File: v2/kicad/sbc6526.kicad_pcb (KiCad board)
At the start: 4 copper layers, 100 x 100 mm, 59 parts, among them J1 Conn_01x10_Female, P1 2k, P2 5k, SW1 UP, SW2 DOWN, SW3 OK, SW4 CANCEL, SW5 RESET, U1 6526, U10 74AC138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

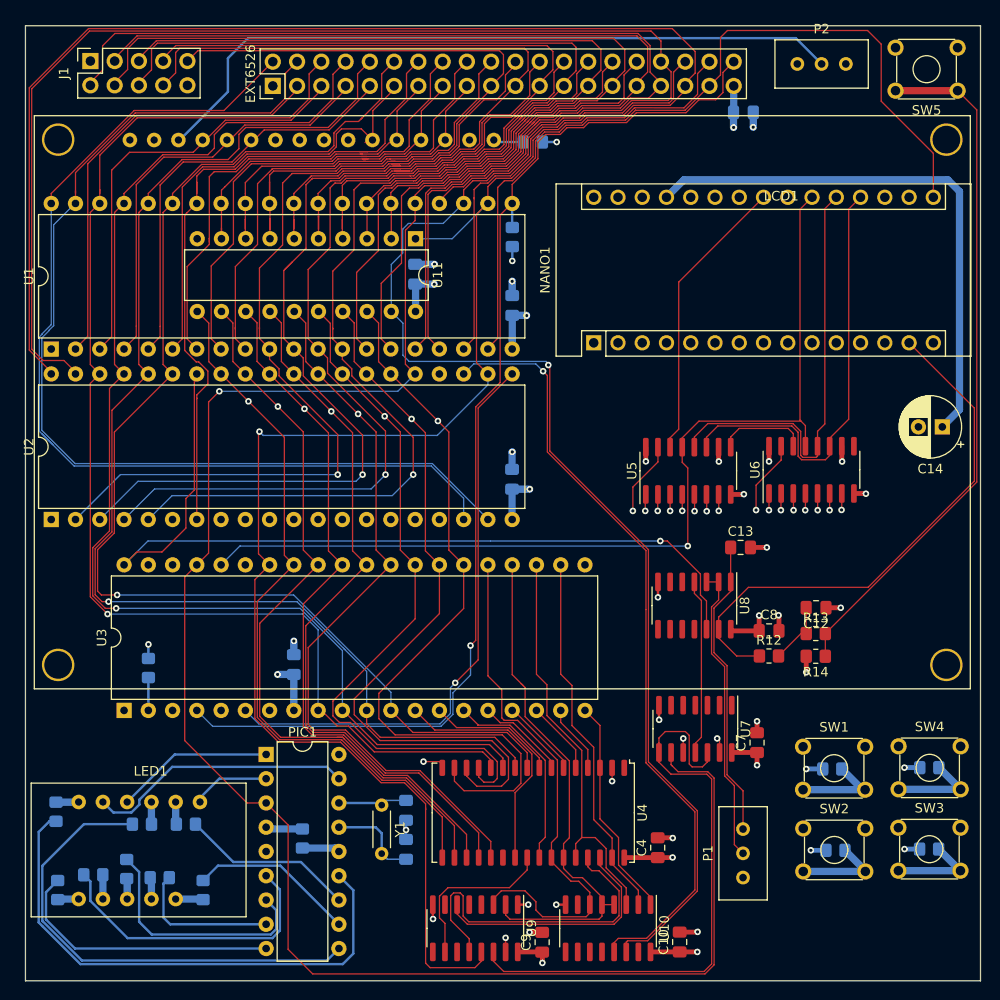
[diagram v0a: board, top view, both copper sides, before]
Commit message: All nets verified
All nets have been verified against all design. Even though v2 is not tested yet, at least, the schematic is correct.
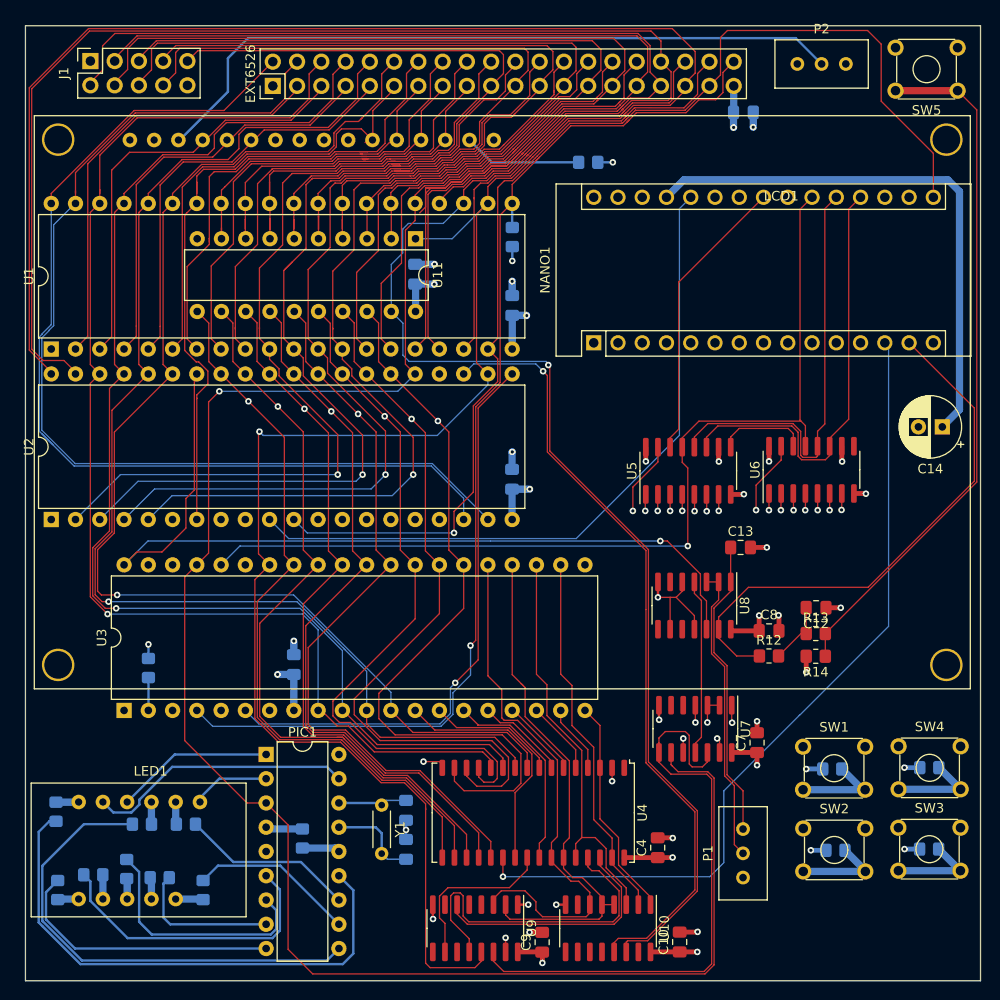
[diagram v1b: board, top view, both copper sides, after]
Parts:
- moved R10 6.18 mm to (158.9, 64.3)
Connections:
- LCD1 pad 15: GND -> Net-(LCD1-Pad15)
- LCD1 pad 16: Net-(LCD1-Pad16) -> GND
- R10 pad 2: Net-(LCD1-Pad16) -> Net-(LCD1-Pad15)
- U7 pad 1: (no net) -> VCC
- U7 pad 2: (no net) -> GND
- U7 pad 3: (no net) -> GND
- U7 pad 4: (no net) -> VCC
- U7 pad 5: (no net) -> Net-(U7-Pad5)
- U7 pad 6: (no net) -> Net-(U7-Pad6)
- U8 pad 10: (no net) -> Net-(U8-Pad10)
- U8 pad 11: (no net) -> GND
- U8 pad 5: (no net) -> GND
- U8 pad 6: (no net) -> Net-(U8-Pad6)
- U8 pad 8: (no net) -> Net-(U8-Pad8)
- U8 pad 9: (no net) -> GND
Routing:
- net /~CE: track 0.00 -> 87.5 mm, vias 0 -> 1
- net /TODENABLE: track 0.00 -> 73.6 mm
- net /TOD: track 86.5 -> 124.6 mm, vias 0 -> 1
- net /io/PB6: track 106.4 -> 121.8 mm
- net GND: track 36.2 -> 50.5 mm, vias 23 -> 24
- net Net-(LCD1-Pad15): track 0.00 -> 12.4 mm
- net VCC: track 130.0 -> 133.7 mm, vias 24 -> 26
- net Net-(LCD1-Pad16): track 3.16 -> 0.00 mm
- net /peripherals/DB6: track 35.6 -> 34.1 mm
- net /io/PB4: track 99.0 -> 97.8 mm
- net /io/PB3: track 145.0 -> 143.9 mm
- net /PHI2: track 210.0 -> 209.0 mm
- net /peripherals/DB7: track 36.1 -> 35.3 mm
- net /io/PB7: track 114.4 -> 113.5 mm
- net /peripherals/DB5: track 37.6 -> 36.8 mm
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
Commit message: new revision - dual 6526
new revision - dual 6526
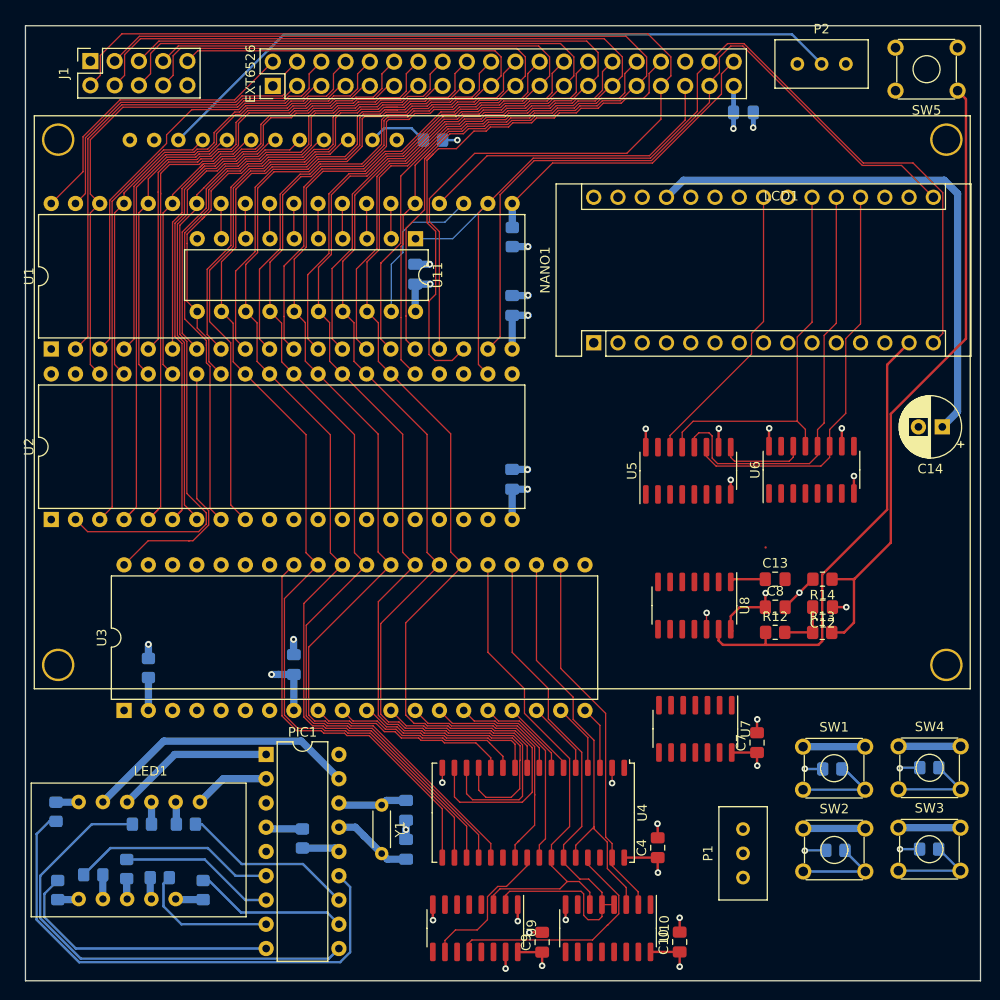
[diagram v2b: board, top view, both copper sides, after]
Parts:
- moved R10 16.4 mm to (142.7, 62.0)
- moved R14 8.10 mm to (183.4, 108.0)
- moved C13 4.92 mm to (178.5, 108.0)
- moved R12 2.56 mm to (178.5, 113.5)
- moved C8 2.56 mm to (178.5, 110.9)
- moved R13 0.68 mm to (183.4, 113.5)
- moved C12 0.68 mm to (183.5, 110.9)
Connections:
- EXT6526 pad 11: /peripherals/LCD_D4 -> /peripherals/PA4
- EXT6526 pad 13: /peripherals/LCD_D5 -> /peripherals/PA5
- EXT6526 pad 15: /peripherals/LCD_D6 -> /peripherals/PA6
- EXT6526 pad 16: /peripherals/DB0 -> /bootstrap/D0
- EXT6526 pad 17: /peripherals/LCD_D7 -> /peripherals/PA7
- EXT6526 pad 18: /peripherals/DB1 -> /bootstrap/D1
- EXT6526 pad 20: /peripherals/DB2 -> /bootstrap/D2
- EXT6526 pad 22: /peripherals/DB3 -> /bootstrap/D3
- EXT6526 pad 24: /peripherals/DB4 -> /bootstrap/D4
- EXT6526 pad 26: /peripherals/DB5 -> /bootstrap/D5
- EXT6526 pad 28: /peripherals/DB6 -> /bootstrap/D6
- EXT6526 pad 30: /peripherals/DB7 -> /bootstrap/D7
- EXT6526 pad 34: /peripherals/~FLAG -> /peripherals/~EXTPC
- EXT6526 pad 35: /peripherals/~PC -> /peripherals/~EXTFLAG
- EXT6526 pad 36: /memory/~CIA -> /memory/~CIAEXT
- EXT6526 pad 5: /peripherals/LCD_RS -> /peripherals/PA1
- EXT6526 pad 7: /peripherals/LCD_RW -> /peripherals/PA2
- EXT6526 pad 9: /peripherals/LCD_E -> /peripherals/PA3
- U1 pad 18: /peripherals/~PC -> /peripherals/~EXTPC
- U1 pad 24: /peripherals/~FLAG -> /peripherals/~EXTFLAG
- U1 pad 3: /peripherals/LCD_RS -> /peripherals/PA1
- U1 pad 4: /peripherals/LCD_RW -> /peripherals/PA2
- U1 pad 5: /peripherals/LCD_E -> /peripherals/PA3
- U1 pad 6: /peripherals/LCD_D4 -> /peripherals/PA4
- U1 pad 7: /peripherals/LCD_D5 -> /peripherals/PA5
- U1 pad 8: /peripherals/LCD_D6 -> /peripherals/PA6
- U1 pad 9: /peripherals/LCD_D7 -> /peripherals/PA7
- U10 pad 12: Net-(U10-Pad12) -> /memory/~CIAEXT
- U2 pad 18: /peripherals/SERCLK -> Net-(U2-Pad18)
- U2 pad 19: /peripherals/SERDAT -> Net-(U2-Pad19)
- U2 pad 2: /io/PB0 -> /peripherals/~CIARES
- U2 pad 3: /io/PB1 -> /peripherals/LCD_RS
- U2 pad 39: /peripherals/~FLAG -> Net-(U2-Pad39)
- U2 pad 4: /io/PB2 -> /peripherals/LCD_RW
- U2 pad 40: /peripherals/~PC -> Net-(U2-Pad40)
- U2 pad 5: /io/PB3 -> /peripherals/LCD_E
- U2 pad 6: Net-(U2-Pad6) -> /peripherals/LCD_D4
- U2 pad 7: /peripherals/~CIARES -> /peripherals/LCD_D5
- U2 pad 8: Net-(U2-Pad8) -> /peripherals/LCD_D6
- U2 pad 9: Net-(U2-Pad9) -> /peripherals/LCD_D7
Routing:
- net /PHI2: track 209.0 -> 52.6 mm, vias 1 -> 0
- net /peripherals/~PC: track 152.5 -> 0.00 mm
- net /peripherals/~FLAG: track 137.6 -> 0.00 mm
- net /memory/~CIA: track 142.0 -> 16.4 mm, vias 1 -> 0
- net /bootstrap/A0: track 187.6 -> 75.4 mm, vias 2 -> 0
- net /bootstrap/A1: track 178.2 -> 70.2 mm, vias 2 -> 0
- net /bootstrap/A3: track 177.0 -> 69.2 mm, vias 2 -> 0
- net /bootstrap/A2: track 178.4 -> 71.3 mm, vias 2 -> 0
- net /R~W: track 214.1 -> 107.2 mm, vias 1 -> 0
- net /io/VPB5: track 108.3 -> 9.72 mm
- net /io/VPB6: track 105.8 -> 9.59 mm
- net /io/VPB4: track 102.8 -> 9.72 mm
- net /~CE: track 87.5 -> 0.00 mm, vias 1 -> 0
- net /~IRQ: track 119.7 -> 33.2 mm, vias 1 -> 0
- net /io/VPB7: track 95.6 -> 9.84 mm
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
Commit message: Changing to Dual CIA
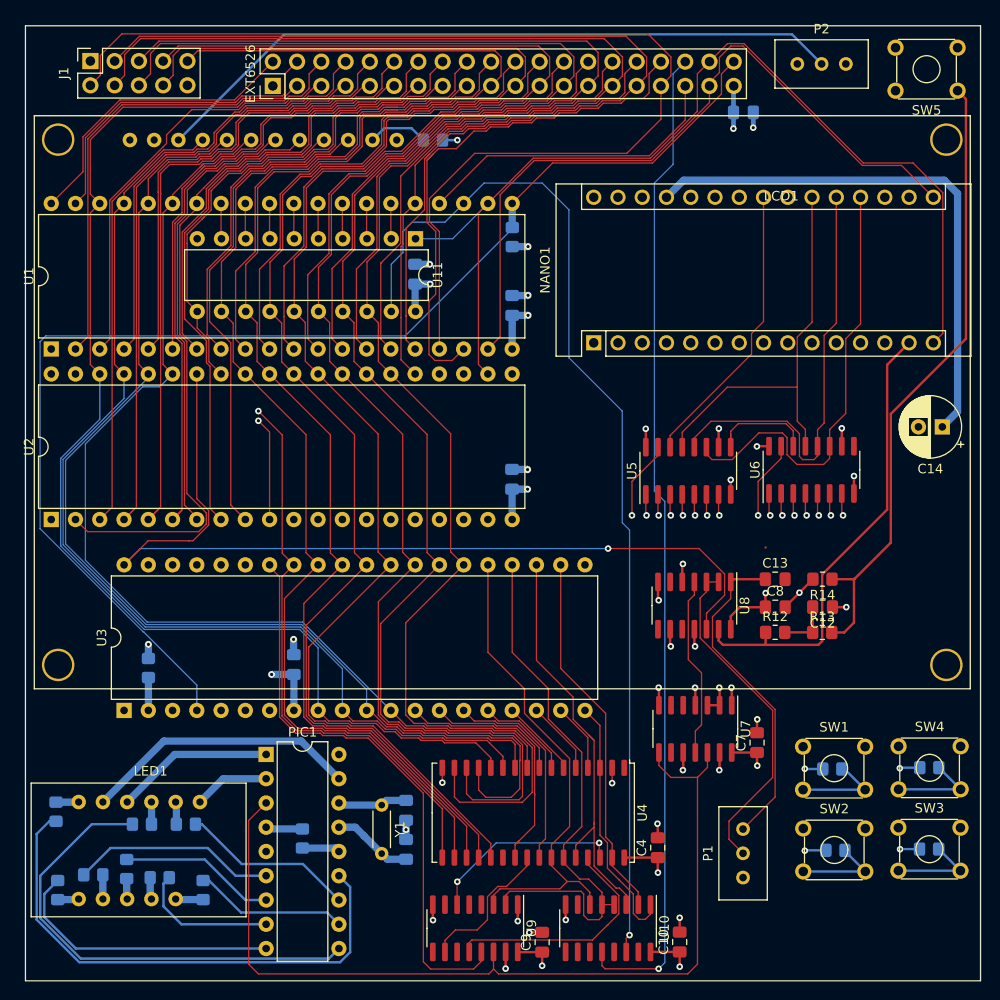
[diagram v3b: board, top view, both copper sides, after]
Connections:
- NANO1 pad 10: /bootstrap/D5 -> /bootstrap/D2
- NANO1 pad 11: /bootstrap/D6 -> /bootstrap/D1
- NANO1 pad 12: /bootstrap/D7 -> /bootstrap/D0
- NANO1 pad 5: /bootstrap/D0 -> /bootstrap/D7
- NANO1 pad 6: /bootstrap/D1 -> /bootstrap/D6
- NANO1 pad 7: /bootstrap/D2 -> /bootstrap/D5
- NANO1 pad 8: /bootstrap/D3 -> /bootstrap/D4
- NANO1 pad 9: /bootstrap/D4 -> /bootstrap/D3
- PIC1 pad 3: /PHI2 -> /clock/~PHI2
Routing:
- net /bootstrap/A0: track 75.4 -> 183.6 mm, vias 0 -> 1
- net /TODENABLE: track 0.00 -> 105.0 mm, vias 0 -> 1
- net /memory/~CIAEXT: track 0.00 -> 104.6 mm, vias 0 -> 1
- net /bootstrap/A3: track 69.2 -> 172.1 mm, vias 0 -> 1
- net /bootstrap/A2: track 71.3 -> 173.9 mm, vias 0 -> 1
- net /bootstrap/A1: track 70.2 -> 172.6 mm, vias 0 -> 1
- net /~IRQ: track 33.2 -> 133.1 mm
- net /clock/~PHI2: track 0.00 -> 96.2 mm
- net /memory/~CIA: track 16.4 -> 110.0 mm, vias 0 -> 1
- net /bootstrap/D0: track 96.8 -> 186.0 mm, vias 0 -> 1
- net /~RES: track 28.7 -> 98.3 mm
- net /bootstrap/D1: track 121.5 -> 187.7 mm
- net /bootstrap/D2: track 119.5 -> 180.4 mm
- net /R~W: track 107.2 -> 167.3 mm
- net /bootstrap/A11: track 6.66 -> 65.1 mm, vias 0 -> 1
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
